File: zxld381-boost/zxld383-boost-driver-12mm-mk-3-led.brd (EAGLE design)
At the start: 12 x 12 mm, 5 parts, among them Q1 MOSFET-NCHANNELIRLML2502

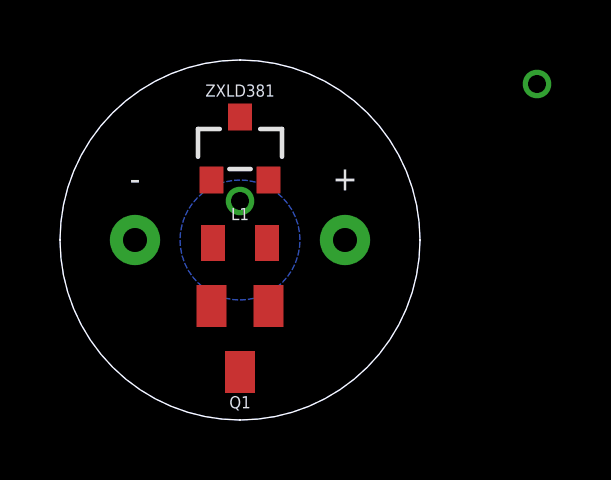
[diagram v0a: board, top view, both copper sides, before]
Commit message: bunch of new zxld38' boards and a third revision of the lm3410 pcb
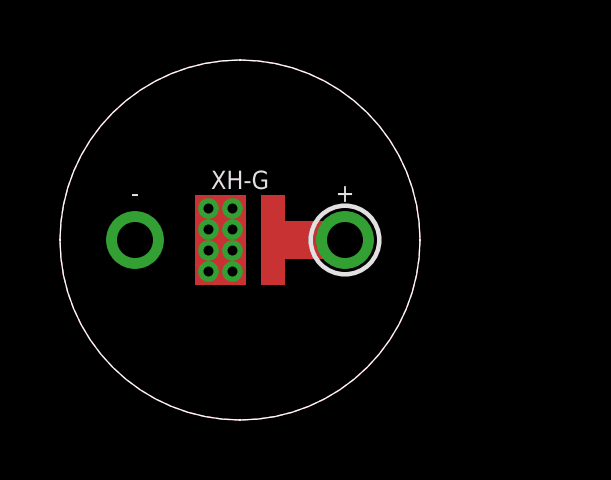
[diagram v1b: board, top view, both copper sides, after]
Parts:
- removed L1: 15uH, A_butts:0805
- removed Q1: MOSFET-NCHANNELIRLML2502, A_butts:SOT23
- removed ZXLD381: ZXLD381, A_butts:SOT23-3
- added XH-G: LEDXH-G, A_butts:CREE-XLAMP-XH-G
- +: value M01PTH-NS-NOTSUCK -> M01PTH-1.2MM; device A_butts:1X01NSATALL -> A_butts:1X01-1.2MM
- -: value M01PTH-NS-NOTSUCK -> M01PTH-1.2MM-NS; device A_butts:1X01NSATALL -> A_butts:1X01-1.2MM-NS
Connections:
- removed net BATT+: L1.1, Q1.1, ZXLD381.1
- removed net BATT-: Q1.3
- removed net LED+: +.1, L1.2, ZXLD381.2
- removed net LED-: -.1, Q1.2, ZXLD381.3
- new net GND: -.P$1, XH-G.K, XH-G.K@1, XH-G.K@2, XH-G.K@3, XH-G.K@4, XH-G.K@5, XH-G.K@6, XH-G.K@7, XH-G.K@8
- new net VCC: +.P$1, XH-G.A
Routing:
- net VCC: track 0.00 -> 2.40 mm
- added copper zone on layer 1, net GND
- added copper zone on layer 16, net GND
- removed copper zone on layer 16, net BATT+
- removed copper zone on layer 16, net BATT-
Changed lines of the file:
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@@
 <layer number="27" name="tValues" color="7" fill="1" visible="yes" active="yes"/>
 <layer number="28" name="bValues" color="7" fill="1" visible="yes" active="yes"/>
-<layer number="29" name="tStop" color="7" fill="3" visible="no" active="yes"/>
-<layer number="30" name="bStop" color="7" fill="6" visible="no" active="yes"/>
-<layer number="31" name="tCream" color="7" fill="4" visible="no" active="yes"/>
-<layer number="32" name="bCream" color="7" fill="5" visible="no" active="yes"/>
-<layer number="33" name="tFinish" color="6" fill="3" visible="no" active="yes"/>
-<layer number="34" name="bFinish" color="6" fill="6" visible="no" active="yes"/>
-<layer number="35" name="tGlue" color="7" fill="4" visible="no" active="yes"/>
-<layer number="36" name="bGlue" color="7" fill="5" visible="no" active="yes"/>
-<layer number="37" name="tTest" color="7" fill="1" visible="no" active="yes"/>
-<layer number="38" name="bTest" color="7" fill="1" visible="no" active="yes"/>
+<layer number="29" name="tStop" color="7" fill="3" visible="yes" active="yes"/>
+<layer number="30" name="bStop" color="7" fill="6" visible="yes" active="yes"/>
+<layer number="31" name="tCream" color="7" fill="4" visible="yes" active="yes"/>
+<layer number="32" name="bCream" color="7" fill="5" visible="yes" active="yes"/>
+<layer number="33" name="tFinish" color="6" fill="3" visible="yes" active="yes"/>
+<layer number="34" name="bFinish" color="6" fill="6" visible="yes" active="yes"/>
+<layer number="35" name="tGlue" color="7" fill="4" visible="yes" active="yes"/>
+<layer number="36" name="bGlue" color="7" fill="5" visible="yes" active="yes"/>
+<layer number="37" name="tTest" color="7" fill="1" visible="yes" active="yes"/>
+<layer number="38" name="bTest" color="7" fill="1" visible="yes" active="yes"/>
 <layer number="39" name="tKeepout" color="4" fill="11" visible="yes" active="yes"/>
 <layer number="40" name="bKeepout" color="1" fill="11" visible="yes" active="yes"/>
@@
 <layer number="42" name="bRestrict" color="1" fill="10" visible="yes" active="yes"/>
 <layer number="43" name="vRestrict" color="2" fill="10" visible="yes" active="yes"/>
-<layer number="44" name="Drills" color="7" fill="1" visible="no" active="yes"/>
-<layer number="45" name="Holes" color="7" fill="1" visible="no" active="yes"/>
-<layer number="46" name="Milling" color="3" fill="1" visible="no" active="yes"/>
-<layer number="47" name="Measures" color="7" fill="1" visible="no" active="yes"/>
+<layer number="44" name="Drills" color="7" fill="1" visible="yes" active="yes"/>
+<layer number="45" name="Holes" color="7" fill="1" visible="yes" active="yes"/>
+<layer number="46" name="Milling" color="3" fill="1" visible="yes" active="yes"/>
+<layer number="47" name="Measures" color="7" fill="1" visible="yes" active="yes"/>
 <layer number="48" name="Document" color="7" fill="1" visible="yes" active="yes"/>
 <layer number="49" name="Reference" color="7" fill="1" visible="yes" active="yes"/>
@@
 <board>
 <plain>
-<wire x1="6" y1="0" x2="0" y2="6" width="0" layer="20" curve="-90"/>
-<wire x1="0" y1="6" x2="6" y2="12" width="0" layer="20" curve="-90"/>
-<wire x1="6" y1="12" x2="12" y2="6" width="0" layer="20" curve="-90"/>
-<wire x1="12" y1="6" x2="6" y2="0" width="0" layer="20" curve="-90"/>
+<wire x1="0" y1="6" x2="6" y2="0" width="0" layer="20" curve="90"/>
+<wire x1="6" y1="0" x2="12" y2="6" width="0" layer="20" curve="90"/>
+<wire x1="12" y1="6" x2="6" y2="12" width="0" layer="20" curve="90"/>
+<wire x1="6" y1="12" x2="0" y2="6" width="0" layer="20" curve="90"/>
 </plain>
 <attributes>
@@
 </autorouter>
 <elements>
-<element name="ZXLD381" library="A_butts" package="SOT23-3" value="ZXLD381" x="6" y="9" smashed="yes">
-<attribute name="NAME" x="6" y="10.778" size="0.4064" layer="25" font="vector" ratio="12" align="bottom-center"/>
-</element>
-<element name="+" library="A_butts" package="1X01NSATALL" value="M01PTH-NS-NOTSUCK" x="9.5" y="6"/>
-<element name="-" library="A_butts" package="1X01NSATALL" value="M01PTH-NS-NOTSUCK" x="2.5" y="6"/>
-<element name="L1" library="A_butts" package="0805" value="15uH" x="6" y="5.9" smashed="yes">
-<attribute name="NAME" x="6" y="6.662" size="0.4064" layer="25" font="vector" ratio="12" align="bottom-center"/>
-</element>
-<element name="Q1" library="A_butts" package="SOT23" value="MOSFET-NCHANNELIRLML2502" x="6" y="2.7" smashed="yes" rot="R180">
-<attribute name="NAME" x="6" y="0.795" size="0.4064" layer="25" font="vector" ratio="12" rot="R180" align="bottom-center"/>
-</element>
+<element name="+" library="A_butts" package="1X01-1.2MM" value="M01PTH-1.2MM" x="9.5" y="6"/>
+<element name="XH-G" library="A_butts" package="CREE-XLAMP-XH-G" value="LEDXH-G" x="6" y="6"/>
+<element name="-" library="A_butts" package="1X01-1.2MM-NS" value="M01PTH-1.2MM-NS" x="2.5" y="6"/>
 </elements>
 <signals>
-<signal name="LED+">
-<contactref element="ZXLD381" pad="2"/>
-<contactref element="L1" pad="2"/>
-<contactref element="+" pad="1"/>
-<wire x1="6.95" y1="8" x2="9.5" y2="6" width="0" layer="19" extent="1-1"/>
-<wire x1="6.9" y1="5.9" x2="6.95" y2="8" width="0" layer="19" extent="1-1"/>
-</signal>
-<signal name="BATT-">
-<contactref element="Q1" pad="3"/>
+<signal name="GND">
+<polygon width="0.1524" layer="1" rank="6">
+<vertex x="6" y="0" curve="-90"/>
+<vertex x="0" y="6" curve="-90"/>
+<vertex x="6" y="12" curve="-90"/>
+<vertex x="12" y="6" curve="-90"/>
+</polygon>
 <polygon width="0.1524" layer="16" rank="6">
 <vertex x="6" y="0" curve="-90"/>
@@
 <vertex x="12" y="6" curve="-90"/>
 </polygon>
-<via x="15.9" y="11.2" extent="1-16" drill="0.6"/>
-<wire x1="15.9" y1="11.2" x2="6" y2="1.6" width="0" layer="19" extent="1-1"/>
+<contactref element="XH-G" pad="K"/>
+<contactref element="-" pad="P$1"/>
+<contactref element="XH-G" pad="K@1"/>
+<contactref element="XH-G" pad="K@2"/>
+<contactref element="XH-G" pad="K@3"/>
+<contactref element="XH-G" pad="K@4"/>
+<contactref element="XH-G" pad="K@5"/>
+<contactref element="XH-G" pad="K@6"/>
+<contactref element="XH-G" pad="K@7"/>
+<contactref element="XH-G" pad="K@8"/>
 </signal>
-<signal name="LED-">
-<contactref element="Q1" pad="2"/>
-<contactref element="ZXLD381" pad="3"/>
-<contactref element="-" pad="1"/>
-<wire x1="2.5" y1="6" x2="5.05" y2="3.8" width="0" layer="19" extent="1-1"/>
-<wire x1="6" y1="10.1" x2="2.5" y2="6" width="0" layer="19" extent="1-1"/>
-</signal>
-<signal name="BATT+">
-<contactref element="ZXLD381" pad="1"/>
-<contactref element="L1" pad="1"/>
-<contactref element="Q1" pad="1"/>
-<polygon width="0.1524" layer="16">
-<vertex x="6" y="8" curve="90"/>
-<vertex x="4" y="6" curve="90"/>
-<vertex x="6" y="4" curve="90"/>
-<vertex x="8" y="6" curve="90"/>
-</polygon>
-<via x="6" y="7.3" extent="1-16" drill="0.6"/>
-<wire x1="6" y1="7.3" x2="5.05" y2="8" width="0" layer="19" extent="1-1"/>
-<wire x1="5.1" y1="5.9" x2="6" y2="7.3" width="0" layer="19" extent="1-1"/>
-<wire x1="6.95" y1="3.8" x2="5.1" y2="5.9" width="0" layer="19" extent="1-1"/>
+<signal name="VCC">
+<contactref element="XH-G" pad="A"/>
+<contactref element="+" pad="P$1"/>
+<wire x1="9.5" y1="6" x2="7.4" y2="6" width="1.27" layer="1"/>
+<wire x1="7.1" y1="6" x2="7.4" y2="6" width="0.4064" layer="1"/>
 </signal>
 </signals>
